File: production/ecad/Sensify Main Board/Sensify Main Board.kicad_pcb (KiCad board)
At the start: 4 copper layers, 150 parts, among them J1 1-2834011-3, J2 1-2834011-2, J3 1332645, J4 0532611271, J5 Screw_Terminal_01x08, J6 Conn_01x02_Socket, J7 Conn_01x02_Socket, J8 Conn_01x02_Socket, J9 Conn_01x02_Socket, Q1 2N700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

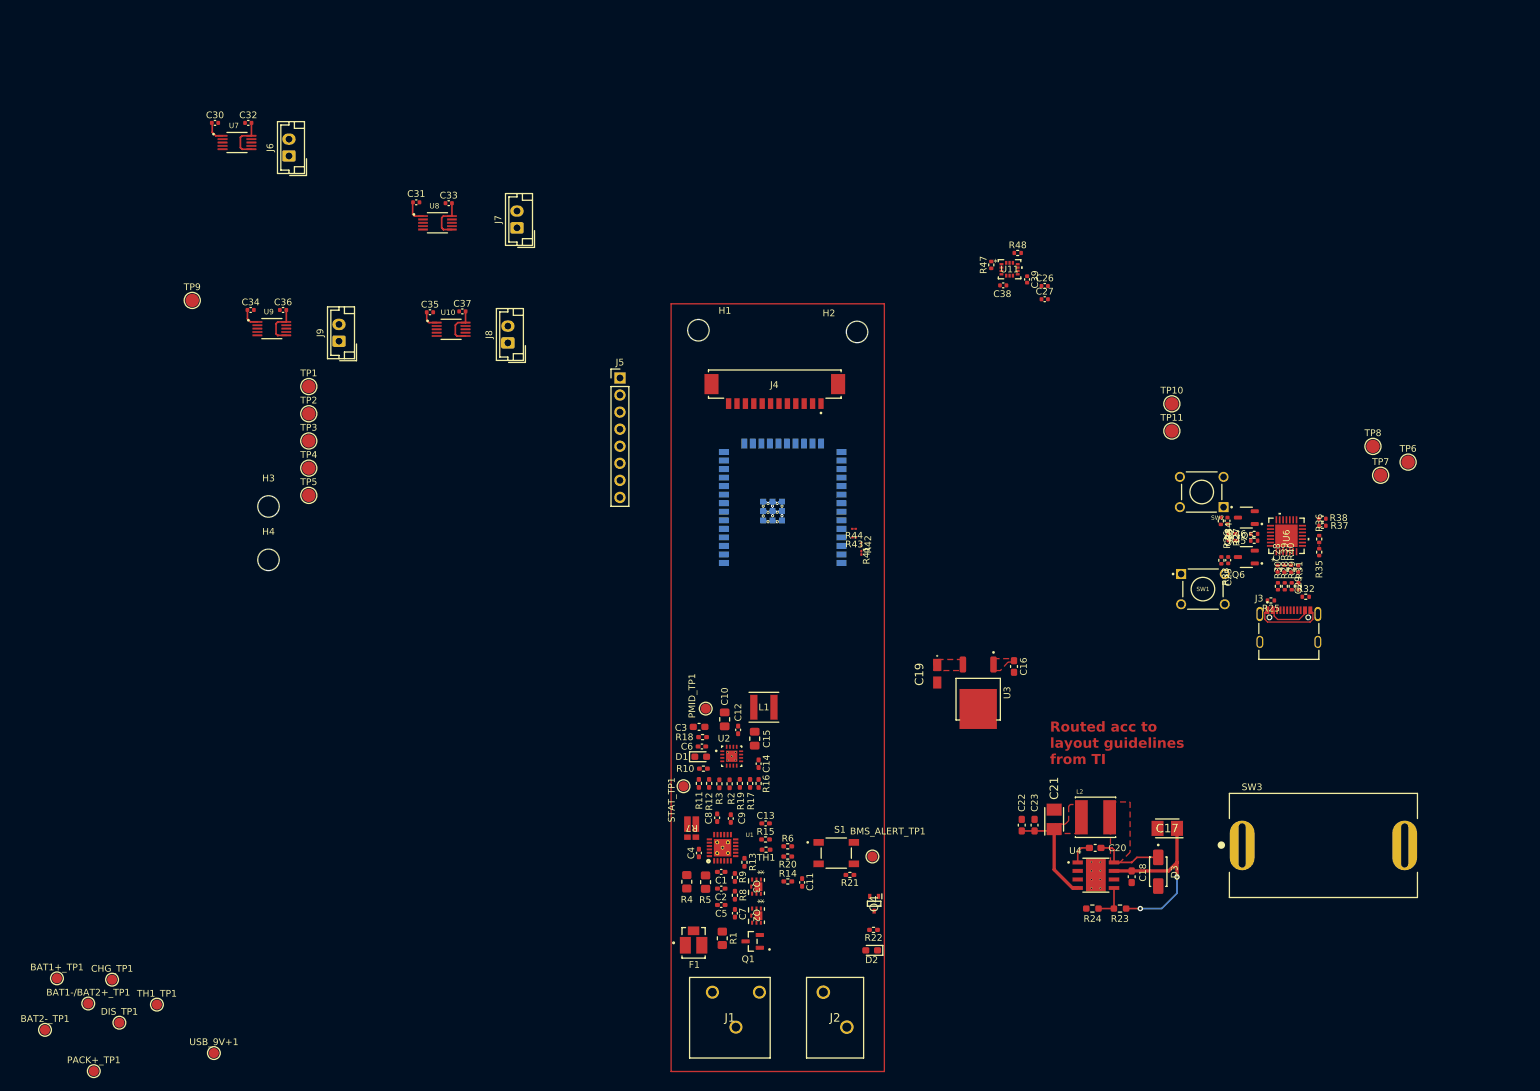
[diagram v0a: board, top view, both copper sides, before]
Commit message: main board layout
finished placing and routing BMS. pours/fills need to be filled in, hasn't been working for me
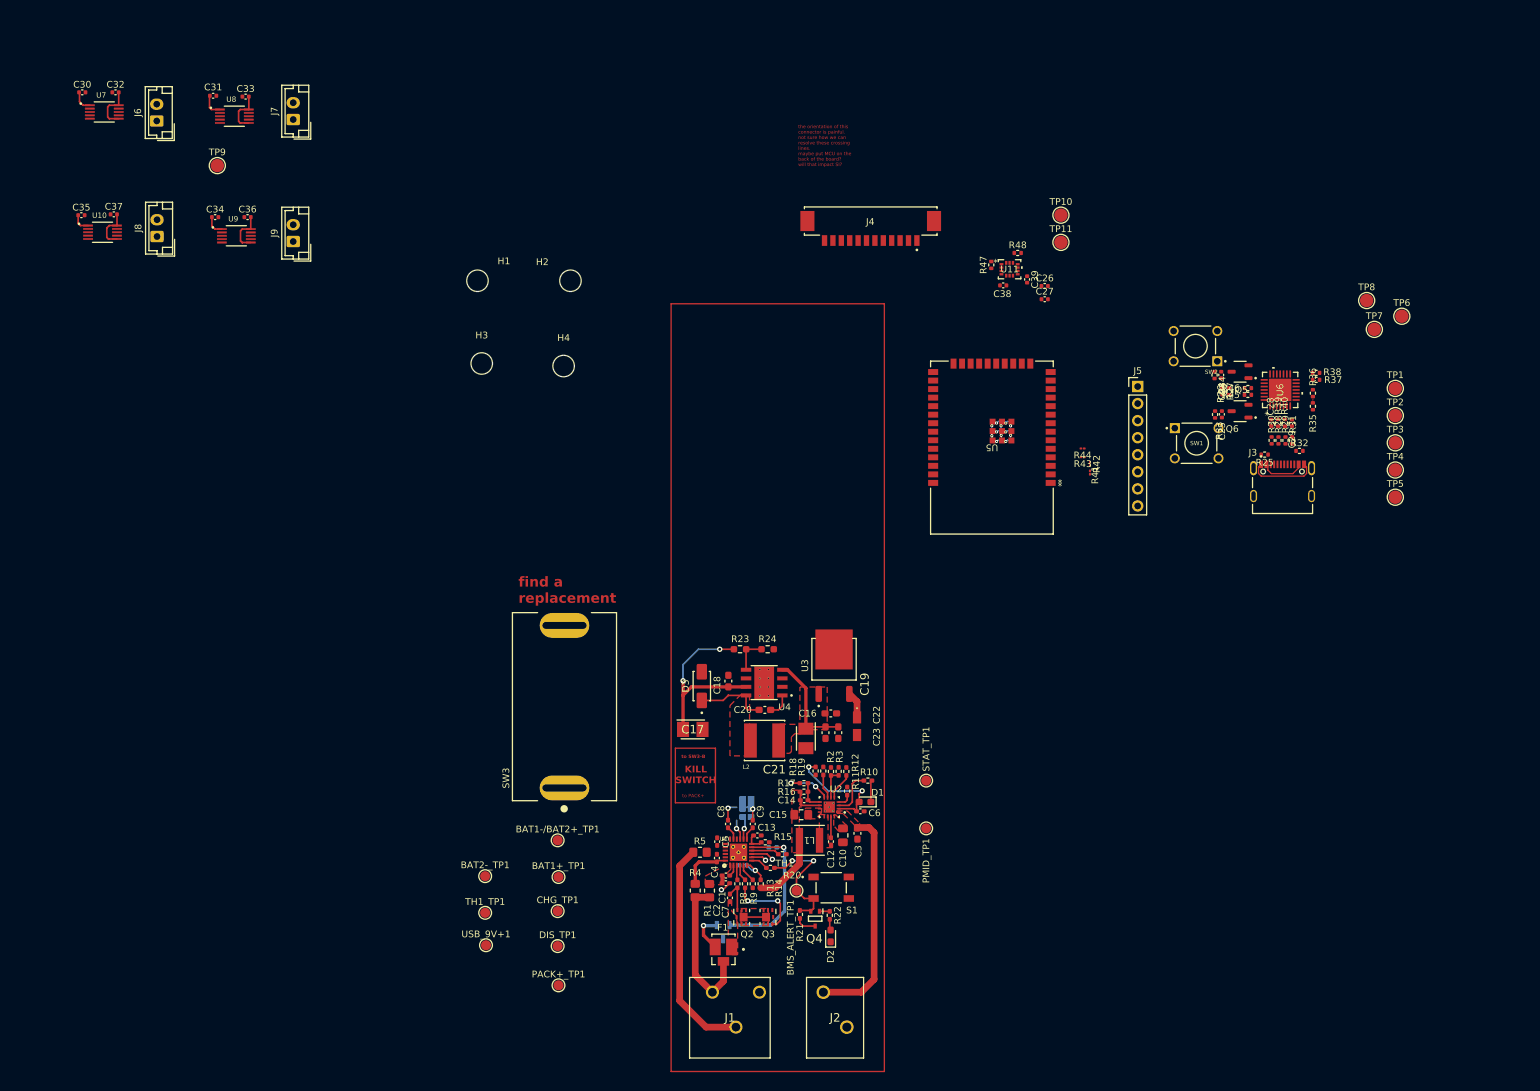
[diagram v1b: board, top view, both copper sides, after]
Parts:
- C11, Q1, R6, R7: moved to B.Cu
- U5: moved to F.Cu
- moved TP1 161.8 mm to (235.3, 82.2)
- moved TP2 161.8 mm to (235.3, 86.2)
- moved TP3 161.8 mm to (235.3, 90.3)
- moved TP4 161.8 mm to (235.3, 94.3)
- moved TP5 161.8 mm to (235.3, 98.4)
- moved SW3 114.9 mm to (111.6, 129.6), turned to 90 degrees
- moved J5 77.1 mm to (197.0, 81.9)
- moved BAT1+_TP1 76.2 mm to (110.7, 154.9)
- moved BAT1-/BAT2+_TP1 74.0 mm to (110.6, 149.5)
- moved D3 73.4 mm to (132.1, 126.5), turned to 90 degrees
- moved C17 72.2 mm to (130.7, 133.0), turned to 0 degrees
- moved PACK+_TP1 70.4 mm to (110.7, 171.1)
- moved BAT2-_TP1 69.4 mm to (99.8, 154.8)
- moved R23 68.5 mm to (137.8, 121.0), turned to 0 degrees
- moved CHG_TP1 67.1 mm to (110.6, 160.0)
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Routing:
- net USB_9V+: track 0.00 -> 33.1 mm
- net BAT1-/BAT2+: track 0.00 -> 33.0 mm
- net Net-(Q1-G): track 0.00 -> 25.6 mm, vias 0 -> 1
- net BAT1+: track 0.00 -> 22.6 mm
- net BMS_ALERT: track 0.00 -> 18.5 mm, vias 0 -> 2
- net REGN: track 0.00 -> 17.1 mm, vias 0 -> 2
- net PACK+: track 0.00 -> 16.3 mm
- net Net-(Q3-G): track 0.00 -> 11.1 mm, vias 0 -> 2
- net GND: track 29.2 -> 36.8 mm, vias 12 -> 15
- net Net-(U1-BATTS): track 0.00 -> 7.50 mm
- net Net-(U2-FB_GND): track 0.00 -> 7.42 mm, vias 0 -> 2
- net +3V3: track 0.18 -> 7.30 mm
- net Net-(U2-STAT): track 0.00 -> 6.89 mm
- net Net-(Q1-D): track 0.00 -> 5.90 mm, vias 0 -> 1
- net Net-(U1-PCKP): track 0.00 -> 4.92 mm, vias 0 -> 1
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- added copper zone on F.Cu, net GND
- added copper zone on F.Cu, net Net-(C12-Pad1)
- added copper zone on F.Cu, net Net-(C7-Pad1)
- added copper zone on F.Cu, net Net-(Q2-D-Pad1)
- added copper zone on F.Cu, net Net-(U1-IN)
- added copper zone on F.Cu, net Net-(U2-PMID)
- added copper zone on F.Cu, net PACK+
- added copper zone on F.Cu, net USB_9V+
- removed copper zone on F.Cu, net +3V3
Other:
- board text added: "KILL SWITCH"
- board text added: "find a replacement"
- board text added: "the orientation of this connector is painful. not sure how we can resolve these crossing lines. maybe put MCU on the back of the board? will that impact SI?"
- board text added: "to PACK+"
- board text added: "to SW3-B"
- board text removed: "Routed acc to layout guidelines from TI"

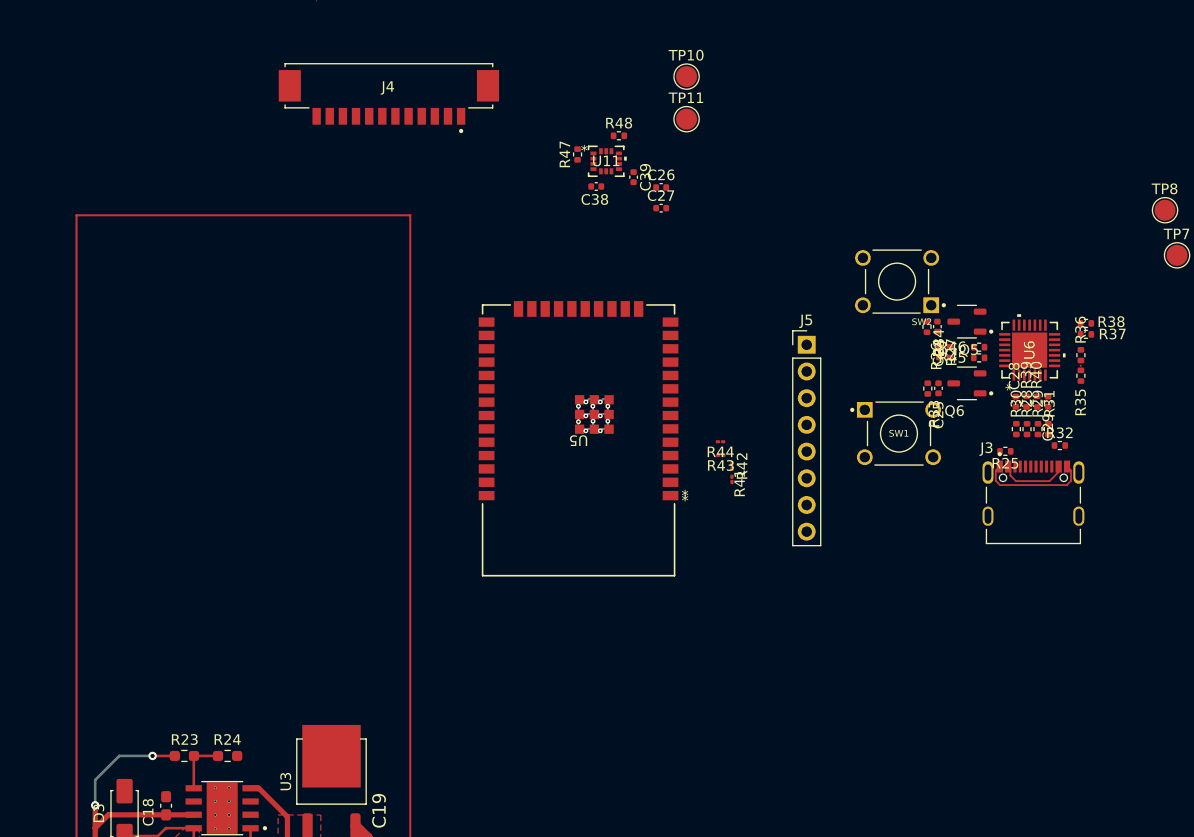
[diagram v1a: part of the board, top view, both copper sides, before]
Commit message: UART Routing
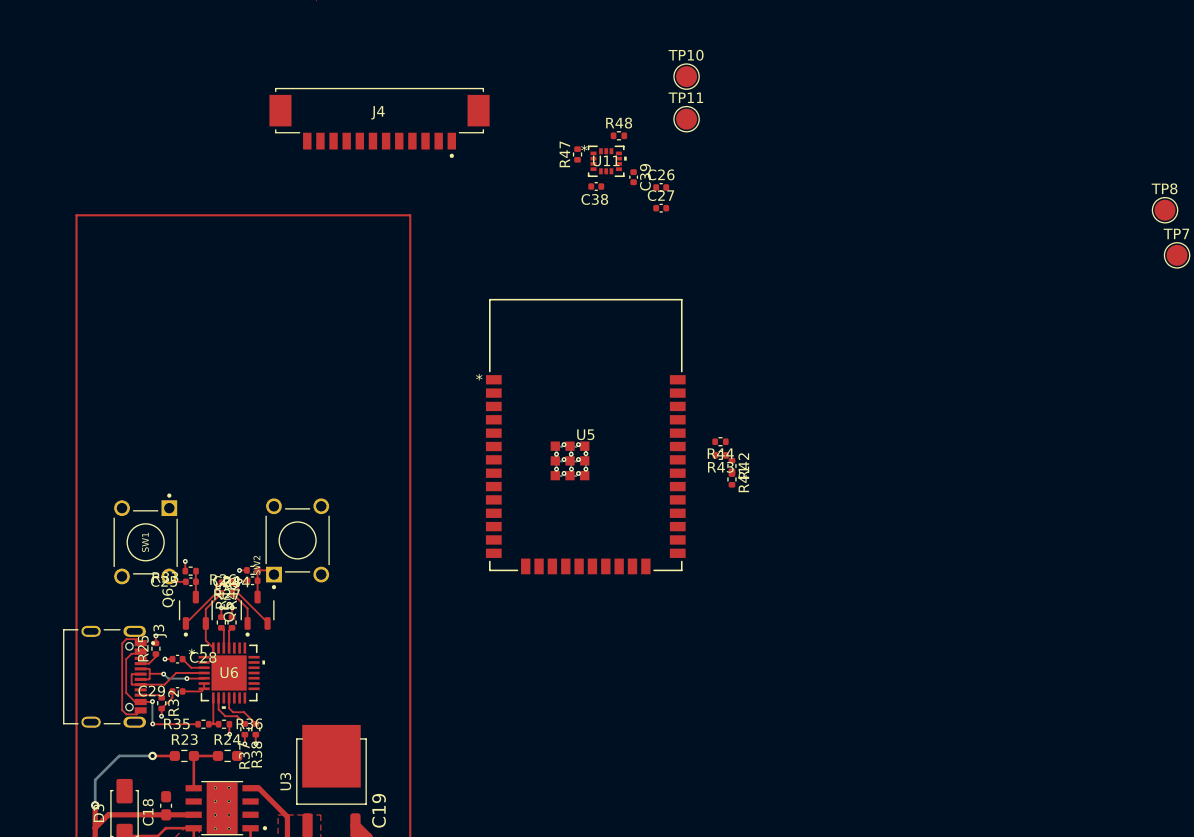
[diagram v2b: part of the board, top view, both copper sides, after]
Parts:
- removed J5: Screw_Terminal_01x08, Connector_PinHeader_2.54mm:PinHeader_1x08_P2.54mm_Vertical
- removed R28, R29, R30, R31, R39, R40: 0, Resistor_SMD:R_0402_1005Metric
- R41, R42, R43, R44: footprint Resistor_SMD:R_01005_0402Metric -> Resistor_SMD:R_0402_1005Metric
- moved R35 89.8 mm to (139.6, 118.0), turned to 0 degrees
- moved R32 88.9 mm to (135.6, 116.0), turned to -90 degrees
- moved R36 88.8 mm to (141.5, 118.0), turned to 0 degrees
- moved R37 88.4 mm to (143.5, 118.5), turned to 90 degrees
- moved J3 88.2 mm to (126.3, 109.0), turned to -90 degrees
- moved R38 87.9 mm to (144.6, 118.5), turned to -90 degrees
- moved C29 87.3 mm to (137.1, 114.9), turned to 180 degrees
- moved C28 83.4 mm to (137.1, 111.8), turned to 0 degrees
- moved R25 83.0 mm to (135.1, 110.8), turned to 90 degrees
- moved U6 82.1 mm to (142.0, 113.1), turned to 0 degrees
- moved Q6 76.5 mm to (138.9, 107.2), turned to 90 degrees
- moved R45 76.4 mm to (141.3, 108.3), turned to 90 degrees
- moved R46 75.8 mm to (142.3, 108.3), turned to 90 degrees
- moved C25 73.5 mm to (138.4, 104.5), turned to 180 degrees
- moved Q5 72.9 mm to (144.7, 107.2), turned to 90 degrees
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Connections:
- J3 pad A6: Net-(J3-DP1) -> USB_D+
- J3 pad A7: Net-(J3-DN1) -> USB_D-
- J3 pad B6: Net-(J3-DP2) -> USB_D+
- J3 pad B7: Net-(J3-DN2) -> USB_D-
- U5 pad 13: IO14 -> unconnected-(U5-IO14-Pad13)
- U5 pad 14: IO12 -> unconnected-(U5-IO12-Pad14)
- U5 pad 6: IO34 -> unconnected-(U5-IO34-Pad6)
- U5 pad 7: IO35 -> unconnected-(U5-IO35-Pad7)
- U5 pad 8: IO32 -> unconnected-(U5-IO32-Pad8)
- U5 pad 9: IO33 -> unconnected-(U5-IO33-Pad9)
- U6 pad 4: Net-(U6-D+) -> USB_D+
- U6 pad 5: Net-(U6-D-) -> USB_D-
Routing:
- net GND: track 36.8 -> 46.4 mm, vias 15 -> 20
- net USB_D+: track 0.00 -> 9.22 mm
- net USB_D-: track 0.00 -> 8.05 mm, vias 0 -> 2
- net FLASHING_VBUS_5V: track 6.65 -> 14.3 mm, vias 0 -> 2
- net DTR: track 0.00 -> 6.12 mm
- net +3V3: track 7.30 -> 13.2 mm, vias 0 -> 4
- net Net-(Q6-Pad1): track 0.00 -> 5.30 mm
- net RTS: track 0.00 -> 5.27 mm
- net Net-(U6-RSTb): track 0.00 -> 4.16 mm
- net Net-(U6-SUSPENDb): track 0.00 -> 4.14 mm
- net EN: track 0.59 -> 4.27 mm
- net Net-(Q5-Pad1): track 0.00 -> 3.47 mm
- net Net-(U6-VBUS): track 0.04 -> 3.49 mm
- net IO0: track 0.03 -> 2.50 mm
- net Net-(J3-CC2): track 0.00 -> 2.11 mm
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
